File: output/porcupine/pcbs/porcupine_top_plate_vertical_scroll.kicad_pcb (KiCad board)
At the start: 2 copper layers, 161.7 x 101.8 mm, 0 parts

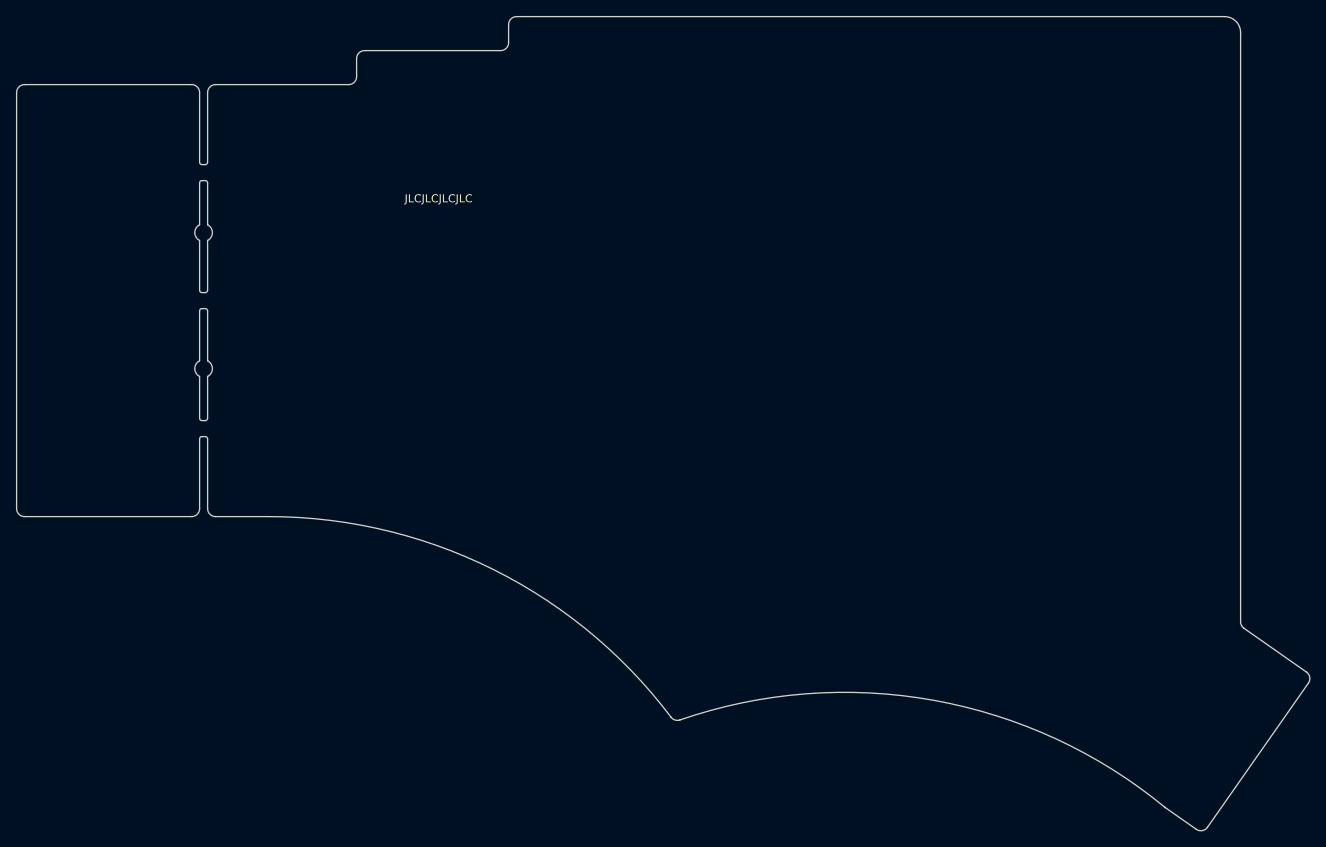
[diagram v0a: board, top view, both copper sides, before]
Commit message: Add both horizontal and vertical scrollbar
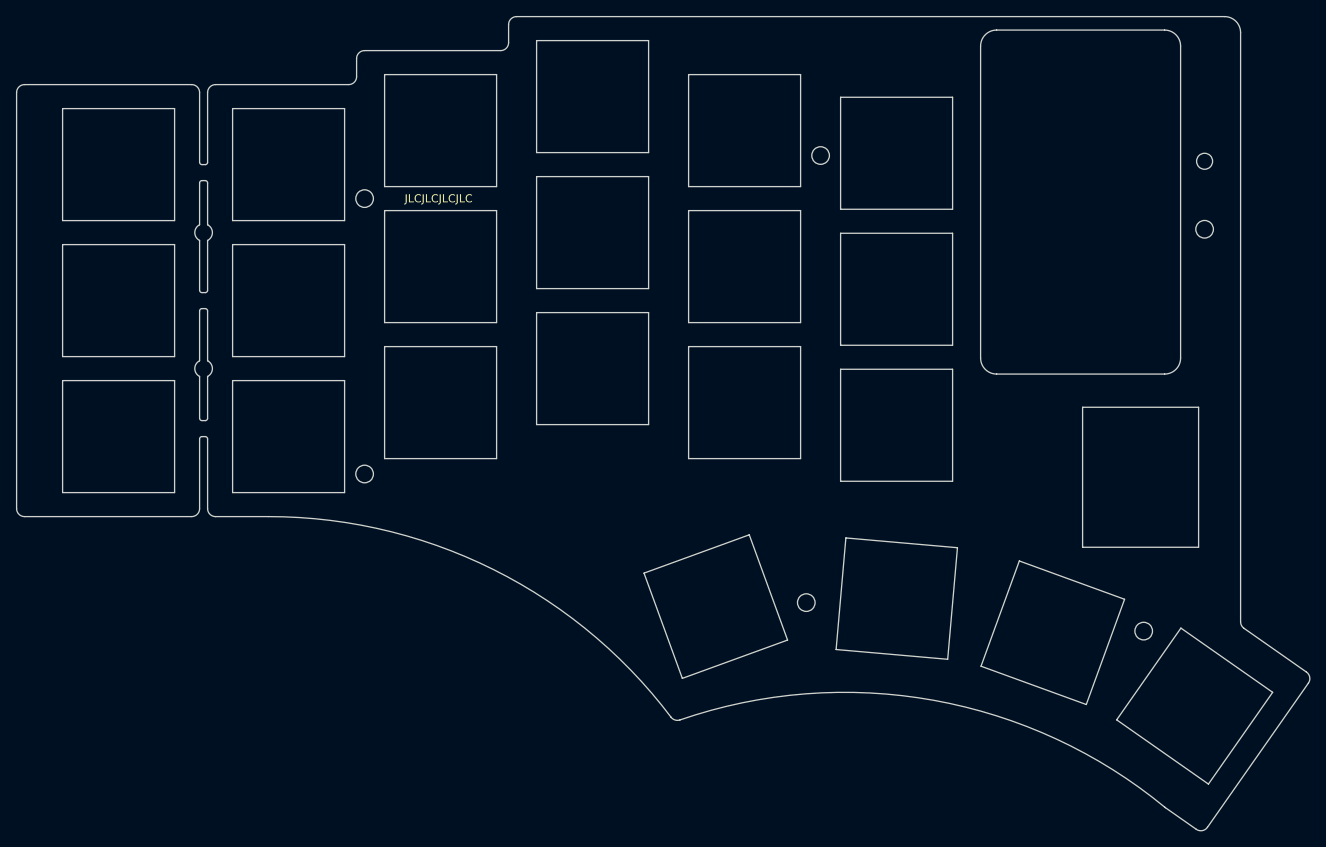
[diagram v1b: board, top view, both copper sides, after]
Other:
- outline, holes or cut-outs redrawn
